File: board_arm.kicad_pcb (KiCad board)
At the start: 2 copper layers, 314.3 x 95.2 mm, 152 parts, among them SW1 SW_SPDT, U1 STM32F072CBT6, U2 PRTR5V0U2X, U3 MCP1725-3302E_SN

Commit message: Add reset cap
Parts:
- added C12: 0.1uF, Capacitor_SMD:C_0805_2012Metric, B.Cu at (357.2, 133.5)
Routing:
- net Net-(U1-Pad45): track 3.66 -> 8.95 mm
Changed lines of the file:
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@@
     (thickness 1.6)
     (drawings 68)
-    (tracks 986)
+    (tracks 987)
     (zones 0)
-    (modules 152)
+    (modules 153)
     (nets 187)
   )
@@
     (solder_mask_min_width 0.25)
     (aux_axis_origin 0 0)
-    (visible_elements 7FFC7FFF)
+    (visible_elements 7FFDFFFF)
     (pcbplotparams
       (layerselection 0x010fc_ffffffff)
@@
     (tags "test point SMD pad")
     (attr virtual)
-    (fp_text reference TP1 (at 0.508 -1.562) (layer F.SilkS)
+    (fp_text reference TP1 (at 0.762 -1.562) (layer F.SilkS)
       (effects (font (size 1 1) (thickness 0.15)))
     )
@@
     (tags SOD-123)
     (attr smd)
-    (fp_text reference D56 (at 0 2 90) (layer B.SilkS)
+    (fp_text reference D56 (at -1.778 2 90) (layer B.SilkS)
       (effects (font (size 1 1) (thickness 0.15)) (justify mirror))
     )
@@
     (tags capacitor)
     (attr smd)
-    (fp_text reference C10 (at 3.67 -0.038 180) (layer F.SilkS)
+    (fp_text reference C10 (at 3.556 0 180) (layer F.SilkS)
       (effects (font (size 1 1) (thickness 0.15)))
     )
@@
     (tags capacitor)
     (attr smd)
-    (fp_text reference C11 (at 3.67 -0.02 180) (layer F.SilkS)
+    (fp_text reference C11 (at 3.556 0 180) (layer F.SilkS)
       (effects (font (size 1 1) (thickness 0.15)))
     )
@@
       (net 53 "Net-(D47-Pad2)"))
   )
+  (module Capacitor_SMD:C_0805_2012Metric (layer B.Cu)
+    (at 357.2025 133.5 180)
+    (descr "Capacitor SMD 0805 (2012 Metric), square (rectangular) end terminal, IPC_7351 nominal, (Body size source: https://docs.google.com/spreadsheets/d/1BsfQQcO9C6DZCsRaXUlFlo91Tg2WpOkGARC1WS5S8t0/edit?usp=sharing), generated with kicad-footprint-generator")
+    (tags capacitor)
+    (attr smd)
+    (fp_text reference C12 (at 0 1.65 180) (layer B.SilkS)
+      (effects (font (size 1 1) (thickness 0.15)) (justify mirror))
+    )
+    (fp_text value 0.1uF (at 0 -1.65 180) (layer B.Fab)
+      (effects (font (size 1 1) (thickness 0.15)) (justify mirror))
+    )
+    (fp_text user %R (at 0 0 180) (layer B.Fab)
+      (effects (font (size 0.5 0.5) (thickness 0.08)) (justify mirror))
+    )
+    (fp_line (start 1.68 -0.95) (end -1.68 -0.95) (layer B.CrtYd) (width 0.05))
+    (fp_line (start 1.68 0.95) (end 1.68 -0.95) (layer B.CrtYd) (width 0.05))
+    (fp_line (start -1.68 0.95) (end 1.68 0.95) (layer B.CrtYd) (width 0.05))
+    (fp_line (start -1.68 -0.95) (end -1.68 0.95) (layer B.CrtYd) (width 0.05))
+    (fp_line (start -0.258578 -0.71) (end 0.258578 -0.71) (layer B.SilkS) (width 0.12))
+    (fp_line (start -0.258578 0.71) (end 0.258578 0.71) (layer B.SilkS) (width 0.12))
+    (fp_line (start 1 -0.6) (end -1 -0.6) (layer B.Fab) (width 0.1))
+    (fp_line (start 1 0.6) (end 1 -0.6) (layer B.Fab) (width 0.1))
+    (fp_line (start -1 0.6) (end 1 0.6) (layer B.Fab) (width 0.1))
+    (fp_line (start -1 -0.6) (end -1 0.6) (layer B.Fab) (width 0.1))
+    (pad 2 smd roundrect (at 0.9375 0 180) (size 0.975 1.4) (layers B.Cu B.Paste B.Mask) (roundrect_rratio 0.25)
+      (net 1 GND))
+    (pad 1 smd roundrect (at -0.9375 0 180) (size 0.975 1.4) (layers B.Cu B.Paste B.Mask) (roundrect_rratio 0.25)
+      (net 99 PWRGD))
+    (model ${KISYS3DMOD}/Capacitor_SMD.3dshapes/C_0805_2012Metric.wrl
+      (at (xyz 0 0 0))
+      (scale (xyz 1 1 1))
+      (rotate (xyz 0 0 0))
+    )
+  )
   (gr_text AT-AT (at 140.208 146.812) (layer F.SilkS)
     (effects (font (size 1 1) (thickness 0.2)))
@@
   (segment (start 355.250482 127.687484) (end 358.468516 127.687484) (width 0.25) (layer F.Cu) (net 118))
   (segment (start 355.250482 127.187484) (end 358.460516 127.187484) (width 0.25) (layer F.Cu) (net 119))
-  (segment (start 353.650482 123.687484) (end 355.6 121.737966) (width 0.25) (layer F.Cu) (net 120))
   (segment (start 353.650482 124.587484) (end 353.650482 123.687484) (width 0.25) (layer F.Cu) (net 120))
   (segment (start 353.150482 122.471568) (end 354.584 121.03805) (width 0.25) (layer F.Cu) (net 121))
@@
   (segment (start 346.550482 126.687484) (end 344.999074 126.687484) (width 0.25) (layer F.Cu) (net 129))
   (segment (start 344.80359 126.492) (end 341.884 126.492) (width 0.25) (layer F.Cu) (net 129))
+  (segment (start 353.650482 123.687484) (end 355.6 121.737966) (width 0.25) (layer F.Cu) (net 120))
   (segment (start 344.602622 127.11598) (end 341.76802 127.11598) (width 0.25) (layer F.Cu) (net 130))
   (segment (start 346.550482 127.187484) (end 344.674126 127.187484) (width 0.25) (layer F.Cu) (net 130))
@@
   (segment (start 344.849518 130.187484) (end 343.465002 131.572) (width 0.25) (layer F.Cu) (net 135))
   (segment (start 346.550482 130.187484) (end 344.849518 130.187484) (width 0.25) (layer F.Cu) (net 135))
+  (segment (start 343.465002 131.572) (end 339.725 135.312002) (width 0.25) (layer F.Cu) (net 135))
   (segment (start 345.122421 130.687484) (end 343.729905 132.08) (width 0.25) (layer F.Cu) (net 136))
   (segment (start 346.550482 130.687484) (end 345.122421 130.687484) (width 0.25) (layer F.Cu) (net 136))

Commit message: Renumber the caps
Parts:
- renumbered C12 to C1, C1 to C3, C6 to C5, C7 to C6, C9 to C7, C10 to C8, C11 to C9

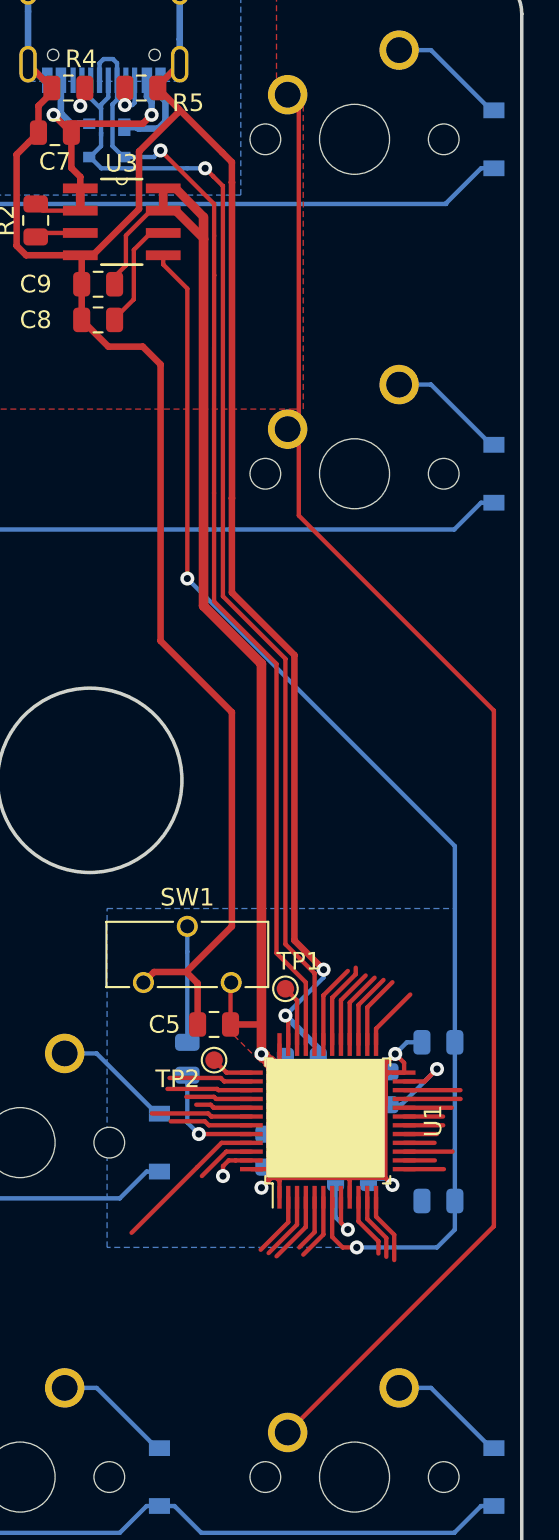
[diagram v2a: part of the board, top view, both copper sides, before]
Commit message: décalage du MCU pour raisons religieuses et décalage de la ligne powergood pour raisons de compliance avec l'USB
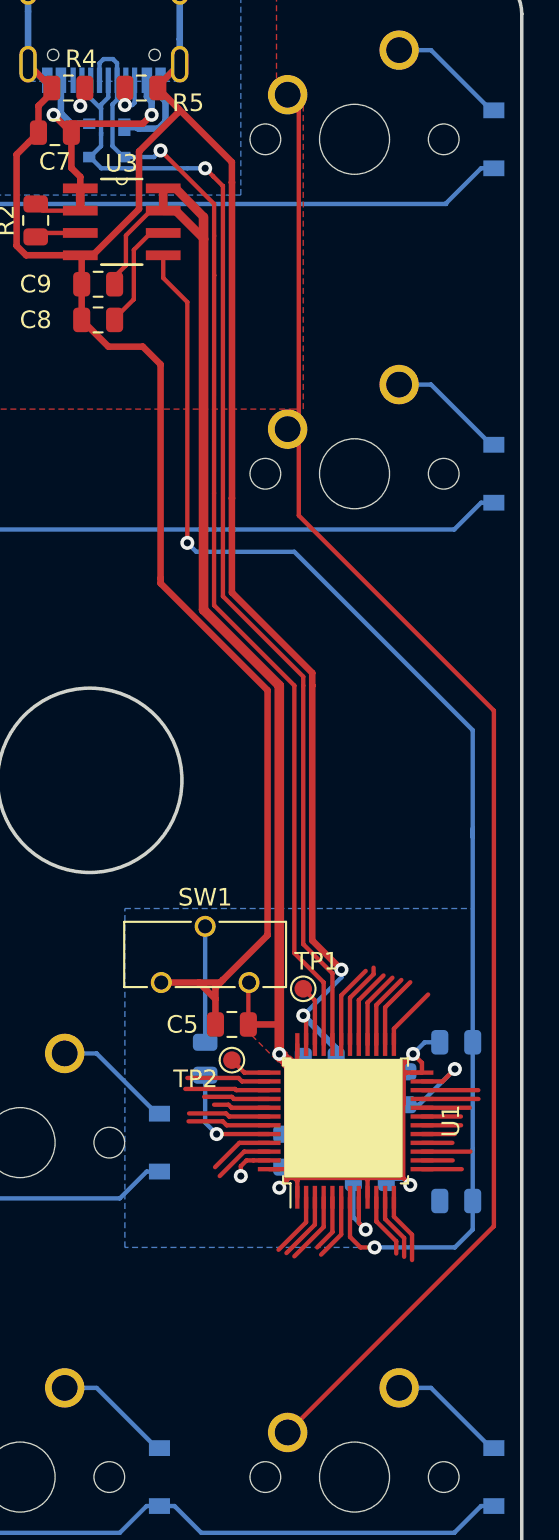
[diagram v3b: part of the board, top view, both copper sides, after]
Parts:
- moved C1 1.02 mm to (358.2, 133.5)
- moved C2 1.02 mm to (348.5, 130.6)
- moved C4 1.02 mm to (350.4, 125.5)
- moved C5 1.02 mm to (345.4, 123.4)
- moved C6 1.02 mm to (353.3, 132.2)
- moved R1 1.02 mm to (343.9, 125.4)
- moved R3 1.02 mm to (358.2, 124.5)
- moved SW1 1.02 mm to (343.9, 119.5)
- moved TP1 1.02 mm to (349.5, 121.4)
- moved TP2 1.02 mm to (345.4, 125.5)
- moved C3 1.02 mm to (355.3, 127.1)
- moved U1 1.02 mm to (351.9, 128.9)
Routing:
- net Net-(U1-Pad45): track 8.95 -> 3.66 mm
- net PWRGD: track 72.3 -> 76.5 mm
- net GND: track 196.8 -> 200.2 mm
- net Net-(U1-Pad42): track 5.74 -> 4.64 mm

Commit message: routage premiere version
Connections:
- K_#1 pad 1: Net-(K_#1-Pad1) -> COL1
- K_#10 pad 1: Net-(K_#10-Pad1) -> COL10
- K_#2 pad 1: Net-(K_#2-Pad1) -> COL2
- K_#3 pad 1: Net-(K_#3-Pad1) -> COL3
- K_#4 pad 1: Net-(K_#4-Pad1) -> COL4
- K_#5 pad 1: Net-(K_#5-Pad1) -> COL5
- K_#6 pad 1: Net-(K_#6-Pad1) -> COL6
- K_#7 pad 1: Net-(K_#7-Pad1) -> COL7
- K_#8 pad 1: Net-(K_#8-Pad1) -> COL8
- K_#9 pad 1: Net-(K_#9-Pad1) -> COL9
- K_'1 pad 1: Net-(K_'1-Pad1) -> COL11
- K_-1 pad 1: Net-(K_-1-Pad1) -> COL11
- K_.1 pad 1: Net-(K_.1-Pad1) -> COL10
- K_/1 pad 1: Net-(K_/1-Pad1) -> COL11
- K_;1 pad 1: Net-(K_;1-Pad1) -> COL10
- K_=1 pad 1: Net-(K_=1-Pad1) -> COL12
- K_A1 pad 1: Net-(K_A1-Pad1) -> COL1
- K_B1 pad 1: Net-(K_B1-Pad1) -> COL6
- K_BACK1 pad 1: Net-(K_BACK1-Pad1) -> COL13
- K_CAPS1 pad 1: Net-(K_CAPS1-Pad1) -> COL0
- K_D1 pad 1: Net-(K_D1-Pad1) -> COL3
- K_DELETE1 pad 1: Net-(K_DELETE1-Pad1) -> COL15
- K_E1 pad 1: Net-(K_E1-Pad1) -> COL3
- K_ENTER1 pad 1: Net-(K_ENTER1-Pad1) -> COL13
- K_ESC1 pad 1: Net-(K_ESC1-Pad1) -> COL0
- K_F1 pad 1: Net-(K_F1-Pad1) -> COL4
- K_G1 pad 1: Net-(K_G1-Pad1) -> COL5
- K_H1 pad 1: Net-(K_H1-Pad1) -> COL6
- K_I1 pad 1: Net-(K_I1-Pad1) -> COL8
- K_INSERT1 pad 1: Net-(K_INSERT1-Pad1) -> COL15
- K_J1 pad 1: Net-(K_J1-Pad1) -> COL7
- K_K1 pad 1: Net-(K_K1-Pad1) -> COL8
- K_L1 pad 1: Net-(K_L1-Pad1) -> COL9
- K_O1 pad 1: Net-(K_O1-Pad1) -> COL9
- K_P1 pad 1: Net-(K_P1-Pad1) -> COL10
- K_Q1 pad 1: Net-(K_Q1-Pad1) -> COL1
- K_R1 pad 1: Net-(K_R1-Pad1) -> COL4
- K_RSHIFT1 pad 1: Net-(K_RSHIFT1-Pad1) -> COL12
- K_S1 pad 1: Net-(K_S1-Pad1) -> COL2
- K_SHIFT1 pad 1: Net-(K_SHIFT1-Pad1) -> COL0
- K_T1 pad 1: Net-(K_T1-Pad1) -> COL5
- K_TAB1 pad 1: Net-(K_TAB1-Pad1) -> COL0
- K_U1 pad 1: Net-(K_U1-Pad1) -> COL7
- K_UP1 pad 1: Net-(K_UP1-Pad1) -> COL14
- K_W1 pad 1: Net-(K_W1-Pad1) -> COL2
- K_Y1 pad 1: Net-(K_Y1-Pad1) -> COL6
- K_Z1 pad 1: Net-(K_Z1-Pad1) -> COL2
- K_[1 pad 1: Net-(K_[1-Pad1) -> COL11
- K_\1 pad 1: Net-(K_\1-Pad1) -> COL13
- K_]1 pad 1: Net-(K_]1-Pad1) -> COL12
- U1 pad 10: Net-(U1-Pad10) -> ROW3
- U1 pad 11: Net-(U1-Pad11) -> ROW4
- U1 pad 13: Net-(U1-Pad13) -> ROW0
- U1 pad 14: Net-(U1-Pad14) -> ROW1
- U1 pad 15: Net-(U1-Pad15) -> ROW2
- U1 pad 18: Net-(U1-Pad18) -> COL15
- U1 pad 19: Net-(U1-Pad19) -> COL7
- U1 pad 20: Net-(U1-Pad20) -> COL6
- U1 pad 21: Net-(U1-Pad21) -> COL5
- U1 pad 22: Net-(U1-Pad22) -> COL4
- U1 pad 25: Net-(U1-Pad25) -> COL3
- U1 pad 26: Net-(U1-Pad26) -> COL2
- U1 pad 27: Net-(U1-Pad27) -> COL1
- U1 pad 28: Net-(U1-Pad28) -> COL0
- U1 pad 39: Net-(U1-Pad39) -> COL13
- U1 pad 40: Net-(U1-Pad40) -> COL14
- U1 pad 41: Net-(U1-Pad41) -> COL12
- U1 pad 42: Net-(U1-Pad42) -> COL11
- U1 pad 43: Net-(U1-Pad43) -> COL10
- U1 pad 45: Net-(U1-Pad45) -> COL9
- U1 pad 46: Net-(U1-Pad46) -> COL8
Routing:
- net COL0: track 85.3 -> 394.9 mm, vias 0 -> 2
- net COL1: track 86.3 -> 373.9 mm, vias 0 -> 2
- net COL2: track 77.2 -> 356.4 mm, vias 0 -> 2
- net COL3: track 67.2 -> 318.2 mm, vias 0 -> 2
- net COL4: track 67.2 -> 306.0 mm, vias 0 -> 2
- net COL5: track 67.2 -> 288.7 mm, vias 0 -> 2
- net COL6: track 87.8 -> 291.9 mm, vias 0 -> 2
- net COL7: track 67.2 -> 254.1 mm, vias 0 -> 2
- net COL8: track 67.2 -> 242.0 mm
- net COL9: track 67.2 -> 229.6 mm
- net COL10: track 89.8 -> 223.7 mm
- net COL11: track 87.8 -> 197.1 mm
- net COL12: track 87.3 -> 171.9 mm
- net (no net): track 1.52 -> 75.7 mm
- net ROW0: track 313.4 -> 376.1 mm, vias 0 -> 1
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
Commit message: petites corrections
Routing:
- net GND: vias 21 -> 20

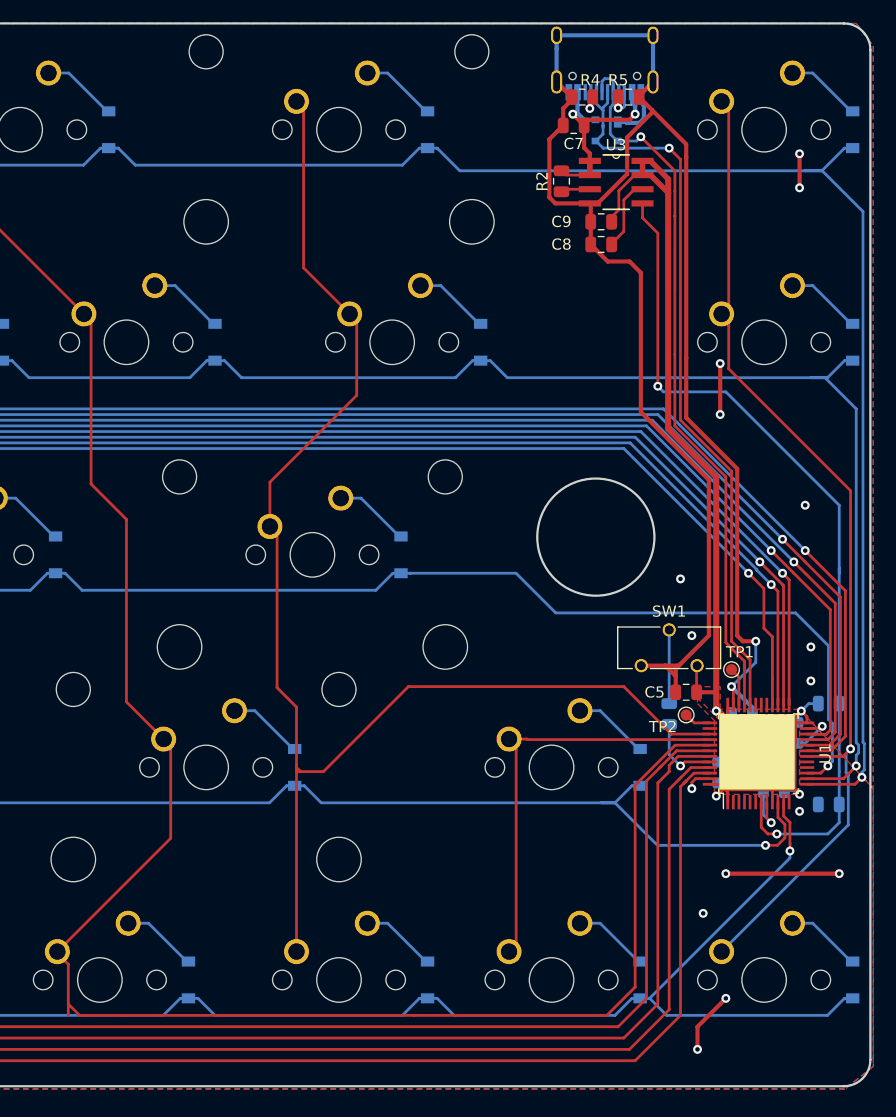
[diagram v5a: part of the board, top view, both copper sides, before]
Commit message: kleine Verbesserungen
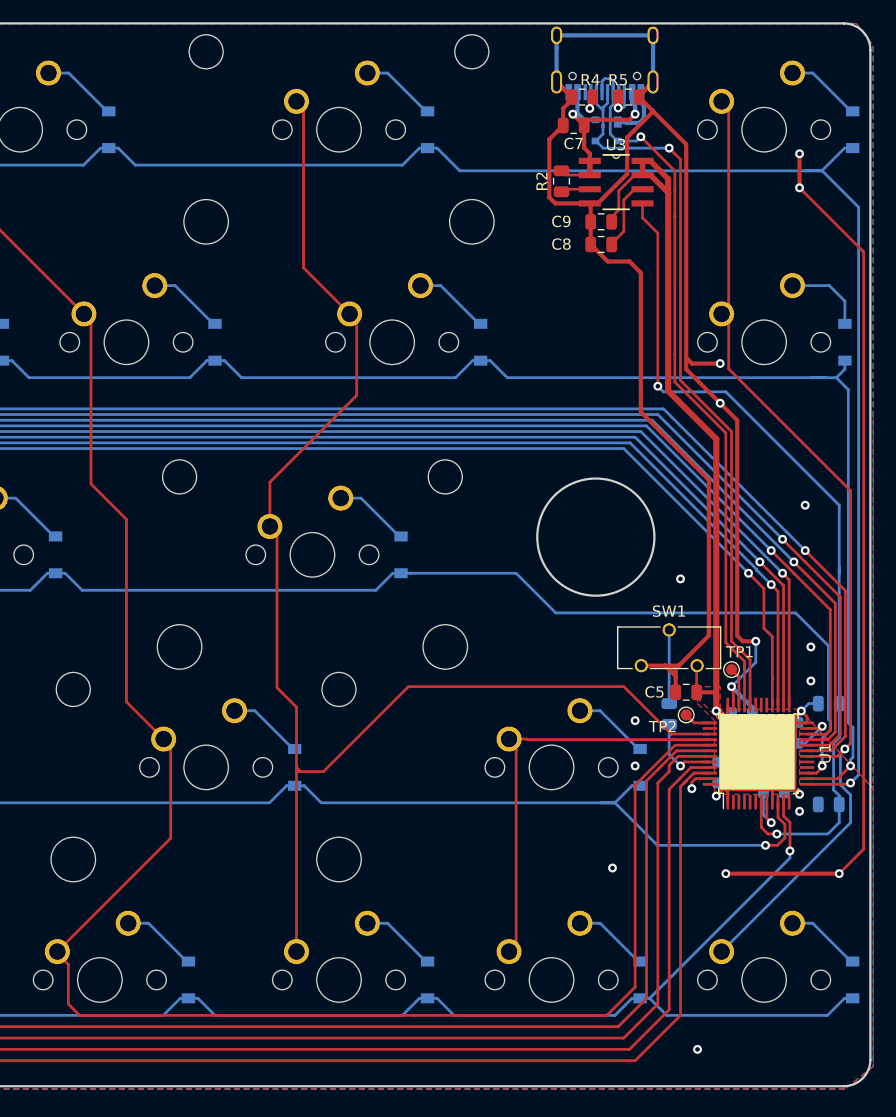
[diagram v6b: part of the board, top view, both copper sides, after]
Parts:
- moved D30 0.70 mm to (359.7, 92.1)
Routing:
- net GND: track 222.9 -> 280.9 mm
- net ROW1: track 350.5 -> 349.1 mm
- net COL12: track 171.9 -> 170.9 mm
- net ROW0: track 376.1 -> 375.4 mm

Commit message: deplacement switch, ajout LED, correction DRC
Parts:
- added LED1: LED, LED_SMD:LED_0805_2012Metric, F.Cu at (352.6, 121.5)
- added R10: 1k, Resistor_SMD:R_0805_2012Metric, F.Cu at (351.0, 116.9)
- SW1: moved to B.Cu
- moved SW1 14.8 mm to (354.6, 109.2), turned to 90 degrees
- moved R1 4.48 mm to (343.9, 120.9)
- moved C7 0.51 mm to (335.4, 73.2)
- moved C8 0.51 mm to (337.8, 83.8)
- moved C9 0.51 mm to (337.8, 81.8)
- moved R2 0.51 mm to (334.3, 78.2)
- moved U2 0.51 mm to (338.3, 73.6)
- moved U3 0.51 mm to (339.2, 78.2)
- moved R5 0.51 mm to (339.8, 70.1)
- moved R4 0.25 mm to (336.4, 70.1)
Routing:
- net GND: track 280.9 -> 174.2 mm, vias 20 -> 17
- net Net-(R1-Pad2): track 6.60 -> 24.8 mm
- net +3V3: track 112.8 -> 118.1 mm, vias 4 -> 5
- net Net-(R1-Pad1): track 6.92 -> 11.6 mm
- net Net-(LED1-Pad1): track 0.00 -> 3.90 mm
- net ROW1: track 349.1 -> 351.9 mm
- net COL2: track 356.4 -> 359.2 mm
- net COL1: track 373.9 -> 376.6 mm
- net COL4: track 306.0 -> 303.4 mm
- net COL0: track 394.9 -> 397.5 mm
- net COL5: track 288.7 -> 286.3 mm
- net COL3: track 318.2 -> 316.0 mm
- net Net-(LED1-Pad2): track 0.00 -> 2.21 mm
- net +5V: track 19.3 -> 20.8 mm
- net Net-(R4-Pad2): track 3.13 -> 4.25 mm
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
